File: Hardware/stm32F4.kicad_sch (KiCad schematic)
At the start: 25 parts, among them J1 USB_C_Receptacle_USB2.0_16P, SW1 Push, SW2 Push, U1 STM32F411CCU6, U2 AMS1117-3.3, U3 SRV05-4, Y1 25MHz

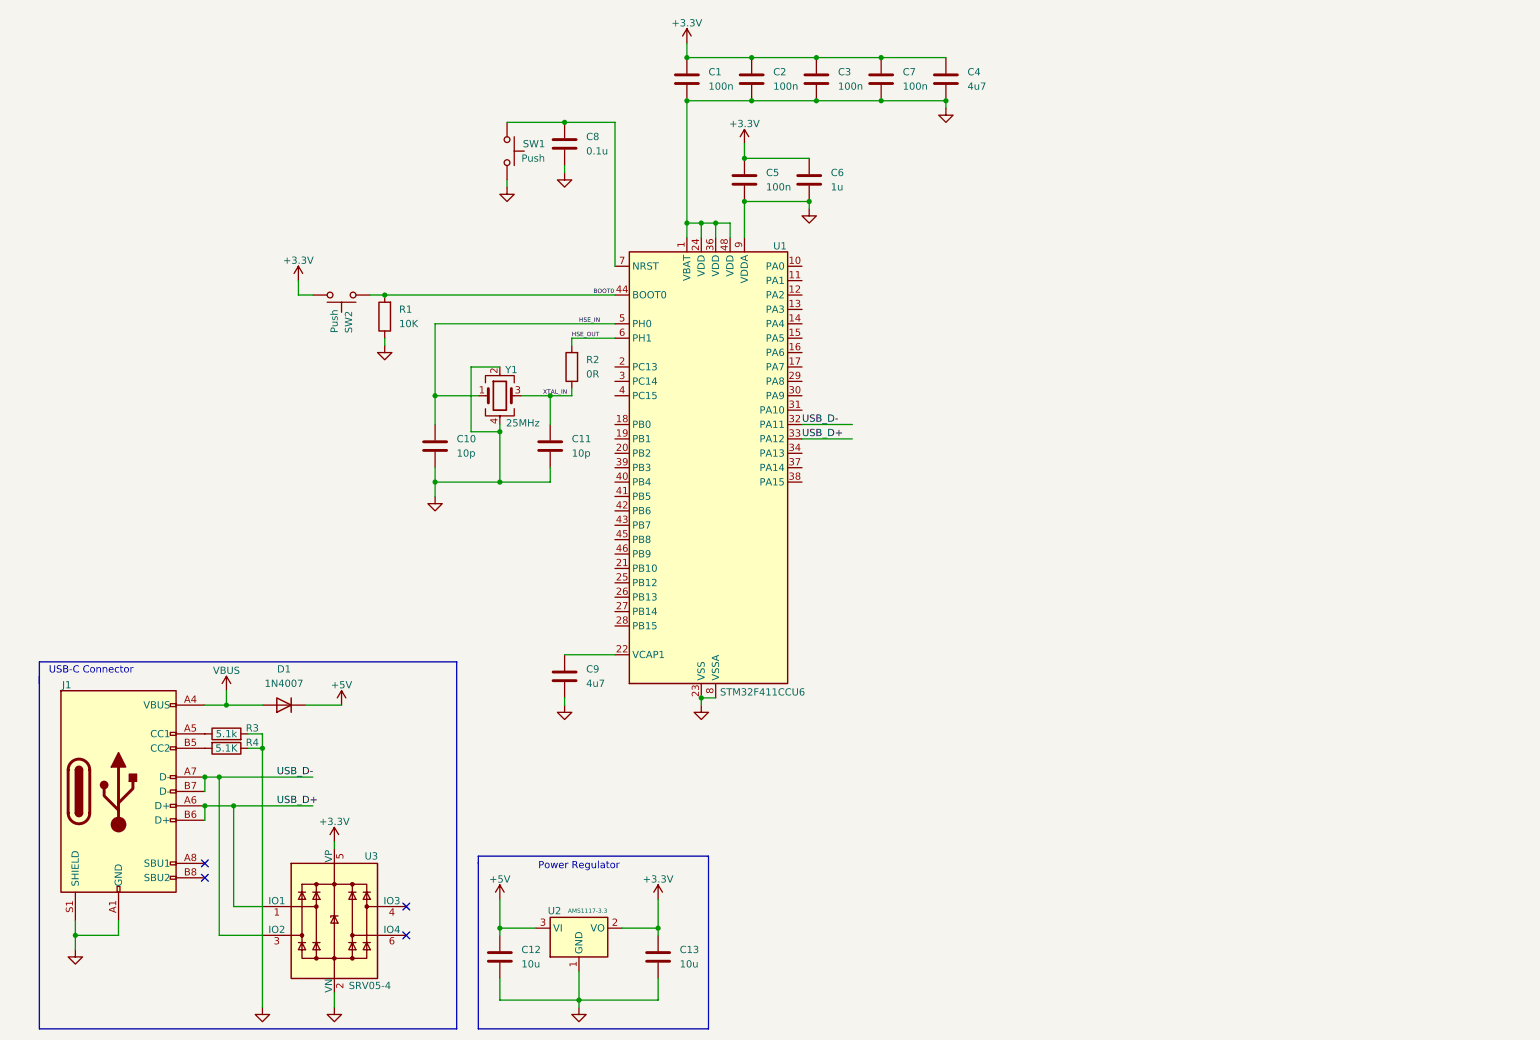
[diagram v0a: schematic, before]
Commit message: Added GPIO Breakout and SWD Conn.
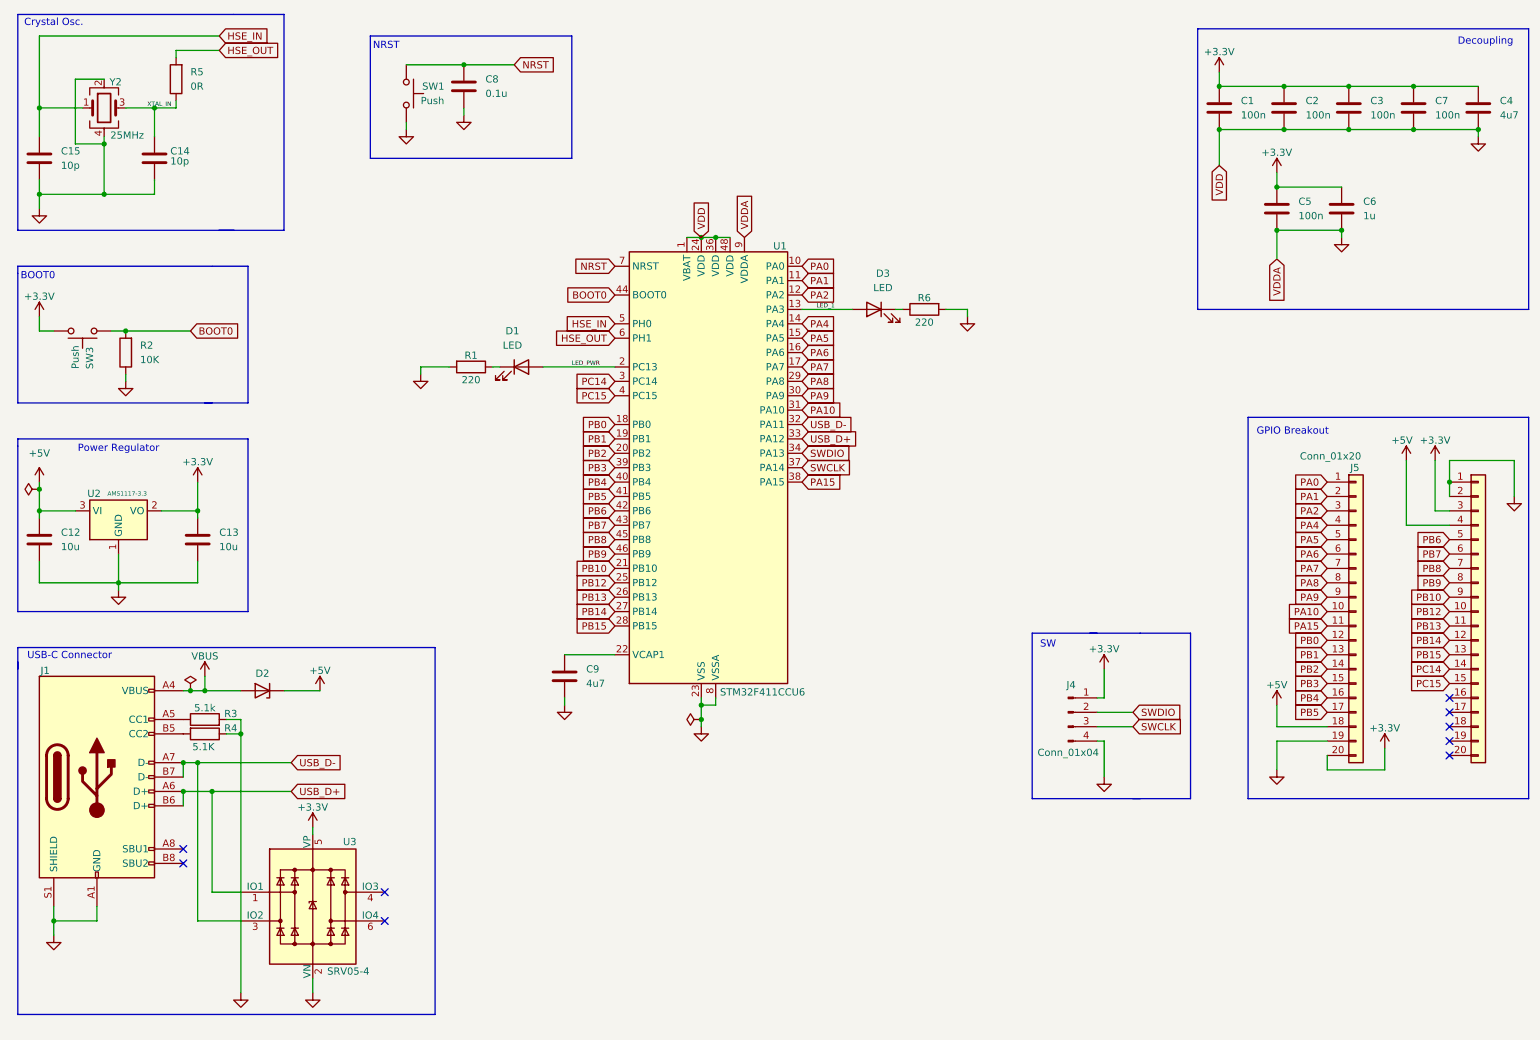
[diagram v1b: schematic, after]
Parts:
- removed C10, C11: 10p, symbol Device:C
- removed D1: 1N4007, Diode_THT:D_DO-41_SOD81_P10.16mm_Horizontal, symbol Diode:1N4007
- removed SW2: Push, symbol Switch:SW_Push
- removed Y1: 25MHz, symbol Device:Crystal_GND24
- added C14, C15: 10p, symbol Device:C
- added D1, D3: LED, symbol Device:LED
- added D2: D_Zener, symbol Device:D_Zener
- added J4: Conn_01x04, Connector_PinHeader_2.54mm:PinHeader_1x04_P2.54mm_Vertical, symbol Connector:Conn_01x04_Pin
- added J5: Conn_01x20, Connector_PinHeader_2.54mm:PinHeader_1x20_P2.54mm_Vertical, symbol Connector_Generic:Conn_01x20
- added J6: Conn_01x20, symbol Connector_Generic:Conn_01x20
- added R5: 0R, symbol Device:R
- added R6: 220, symbol Device:R
- added SW3: Push, symbol Switch:SW_Push
- added Y2: 25MHz, symbol Device:Crystal_GND24
- R1: value 10K -> 220
- R2: value 0R -> 10K
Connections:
- net +3.3V: now also J4.1 (Pin_1), J5.20 (Pin_20), J6.3 (Pin_3), SW3.2
- net +5V: now also D2.1 (K), J5.18 (Pin_18), J6.4 (Pin_4)
- net BOOT0: now also R2.2, SW3.1; no longer R1.2
- net GND: now also R1.2, R2.1, C14.2, C15.2, J4.4 (Pin_4), J5.19 (Pin_19), J6.1 (Pin_1), J6.2 (Pin_2), R6.2, Y2.2, Y2.4; no longer R1.1
- net HSE_IN: now also C15.1, Y2.1
- net HSE_OUT: now also R5.2; no longer R2.2
- net VBUS: now also D2.2 (A)
- net XTAL_IN: now also C14.1, R5.1, Y2.3; no longer R2.1
- net NRST: now reaches C8.2, SW1.1, U1.7 (NRST)
- net PA0: now reaches U1.10 (PA0)
- net PA0: now also J5.1 (Pin_1)
- net PA1: now reaches U1.11 (PA1)
- net PA1: now also J5.2 (Pin_2)
- net PA2: now reaches U1.12 (PA2)
- net PA2: now also J5.3 (Pin_3)
- net LED_1: now reaches U1.13 (PA3)
- net LED_1: now also D3.2 (A)
- net PA4: now reaches U1.14 (PA4)
- net PA4: now also J5.4 (Pin_4)
- net PA5: now reaches U1.15 (PA5)
- net PA5: now also J5.5 (Pin_5)
- net PA6: now reaches U1.16 (PA6)
- net PA6: now also J5.6 (Pin_6)
- net PA7: now reaches U1.17 (PA7)
- net PA7: now also J5.7 (Pin_7)
- net PB0: now reaches U1.18 (PB0)
- net PB0: now also J5.12 (Pin_12)
- net PB1: now reaches U1.19 (PB1)
- net PB1: now also J5.13 (Pin_13)
- net LED_PWR: now reaches U1.2 (PC13)
- net LED_PWR: now also D1.2 (A)
- net PB2: now reaches U1.20 (PB2)
- net PB2: now also J5.14 (Pin_14)
- net PB10: now reaches U1.21 (PB10)
- net PB10: now also J6.9 (Pin_9)
- net PB12: now reaches U1.25 (PB12)
- net PB12: now also J6.10 (Pin_10)
- net PB13: now reaches U1.26 (PB13)
- net PB13: now also J6.11 (Pin_11)
- net PB14: now reaches U1.27 (PB14)
- net PB14: now also J6.12 (Pin_12)
- net PB15: now reaches U1.28 (PB15)
- net PB15: now also J6.13 (Pin_13)
- net PA8: now reaches U1.29 (PA8)
- net PA8: now also J5.8 (Pin_8)
- net PC14: now reaches U1.3 (PC14)
- net PC14: now also J6.14 (Pin_14)
- net PA9: now reaches U1.30 (PA9)
- net PA9: now also J5.9 (Pin_9)
- net PA10: now reaches U1.31 (PA10)
- net PA10: now also J5.10 (Pin_10)
- net SWDIO: now reaches U1.34 (PA13)
- net SWDIO: now also J4.2 (Pin_2)
- net SWCLK: now reaches U1.37 (PA14)
- net SWCLK: now also J4.3 (Pin_3)
- net PA15: now reaches U1.38 (PA15)
- net PA15: now also J5.11 (Pin_11)
- net PB3: now reaches U1.39 (PB3)
- net PB3: now also J5.15 (Pin_15)
- net PC15: now reaches U1.4 (PC15)
- net PC15: now also J6.15 (Pin_15)
- net PB4: now reaches U1.40 (PB4)
- net PB4: now also J5.16 (Pin_16)
- net PB5: now reaches U1.41 (PB5)
- net PB5: now also J5.17 (Pin_17)
- net PB6: now reaches U1.42 (PB6)
- net PB6: now also J6.5 (Pin_5)
- net PB7: now reaches U1.43 (PB7)
- net PB7: now also J6.6 (Pin_6)
- net PB8: now reaches U1.45 (PB8)
- net PB8: now also J6.7 (Pin_7)
- net PB9: now reaches U1.46 (PB9)
- net PB9: now also J6.8 (Pin_8)
- new net: D3.1 (K), R6.1
- new net: D1.1 (K), R1.1
- no-connect marks 4 -> 9
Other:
- note added: "BOOT0"
- note added: "Crystal Osc."
- note added: "Decoupling"
- note added: "GPIO Breakout"
- note added: "NRST"
- note added: "SW"
- title: (none) -> STM32F411 Project
- moved on the sheet: C1, C12, C13, C2, C3, C4, C5, C6, C7, C8, J1, R3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

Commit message: Added Footprints and Parts list
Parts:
- removed D2: D_Zener, symbol Device:D_Zener
- removed J4: Conn_01x04, Connector_PinHeader_2.54mm:PinHeader_1x04_P2.54mm_Vertical, symbol Connector:Conn_01x04_Pin
- removed R5: 0R, symbol Device:R
- removed U3: SRV05-4, Package_TO_SOT_SMD:SOT-23-6, symbol Power_Protection:SRV05-4
- added J2: Conn_01x04, Connector_PinHeader_2.54mm:PinHeader_1x04_P2.54mm_Vertical, symbol Connector_Generic:Conn_01x04
- added U4: 2SC6, Package_TO_SOT_SMD:SOT-23-6, symbol Power_Protection:USBLC6-2SC6
- C1, C2, C3, C5, C7: footprint (none) -> Capacitor_SMD:C_0402_1005Metric; Distributor Link (none) -> https://www.digikey.com/en/products/detail/kyocera-avx/0402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; Manufacturer (none) -> KYOCERA AVX; Manufacturer Part Number (none) -> 04023C104KAT2A-62
- C12, C13: footprint (none) -> Capacitor_SMD:C_0402_1005Metric; Distributor Link (none) -> https://www.digikey.com/en/products/detail/nextgen-componen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; Manufacturer (none) -> Aillen; Manufacturer Part Number (none) -> 0402W106M6R3HI
- C14: value 10p -> 18p; footprint (none) -> Capacitor_SMD:C_0603_1608Metric; Distributor Link (none) -> https://www.digikey.com/en/products/detail/nextgen-componen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; Manufacturer (none) -> NextGen Components; Manufacturer Part Number (none) -> 0603N180J500SD
- C15: value 10p -> 18p; footprint (none) -> Capacitor_SMD:C_0402_1005Metric; Distributor Link (none) -> https://www.digikey.com/en/products/detail/nextgen-componen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; Manufacturer (none) -> NextGen Components; Manufacturer Part Number (none) -> 0603N180J500SD
- C4, C9: footprint (none) -> Capacitor_SMD:C_0603_1608Metric; Distributor Link (none) -> https://www.digikey.com/en/products/detail/tdk-corporation/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; Manufacturer (none) -> TDK Corporation; Manufacturer Part Number (none) -> C1608X5R1C475K080AC
- C6: footprint (none) -> Capacitor_SMD:C_0402_1005Metric; Distributor Link (none) -> https://www.digikey.com/en/products/detail/nextgen-componen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; Manufacturer (none) -> Aillen; Manufacturer Part Number (none) -> 0402W105K100HI
- C8: footprint (none) -> Capacitor_SMD:C_0402_1005Metric; Distributor Link (none) -> https://www.digikey.com/en/products/detail/nextgen-componen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; Manufacturer (none) -> Aillen; Manufacturer Part Number (none) -> 0402B104K160HI
- D1, D3: footprint (none) -> LED_SMD:LED_0402_1005Metric; Distributor Link (none) -> https://www.digikey.com/en/products/detail/yongyu-optoelect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; Manufacturer (none) -> Yongyu Optoelectronics; Manufacturer Part Number (none) -> YY0402RE-NN2S0-T1AR4
- J1: footprint (none) -> Connector_USB:USB_C_Receptacle_GCT_USB4105-xx-A_16P_TopMnt_Horizontal; Distributor Link (none) -> https://www.digikey.com/en/products/detail/gct/USB4105-GF-A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; Manufacturer (none) -> GCT; Manufacturer Part Number (none) -> USB4105-GF-A
- J5: Distributor Link (none) -> https://www.digikey.com/en/products/detail/adam-tech/PH1-20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; Manufacturer (none) -> Adam Tech; Manufacturer Part Number (none) -> PH1-20-UA
- J6: footprint (none) -> Connector_PinHeader_2.54mm:PinHeader_1x20_P2.54mm_Vertical; Distributor Link (none) -> https://www.digikey.com/en/products/detail/adam-tech/PH1-20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; Manufacturer (none) -> Adam Tech; Manufacturer Part Number (none) -> PH1-20-UA
- R1, R6: footprint (none) -> Resistor_SMD:R_0402_1005Metric; Distributor Link (none) -> https://www.digikey.com/en/products/detail/yageo/RC0402FR-0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; Manufacturer (none) -> YAGEO; Manufacturer Part Number (none) -> RC0402FR-07221RL
- R2: footprint (none) -> Resistor_SMD:R_0402_1005Metric; Distributor Link (none) -> https://www.digikey.com/en/products/detail/yageo/RC0402JR-0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; Manufacturer (none) -> YAGEO; Manufacturer Part Number (none) -> RC0402JR-0710KL
- R3, R4: footprint (none) -> Resistor_SMD:R_0402_1005Metric; Distributor Link (none) -> https://www.digikey.com/en/products/detail/yageo/RC0402FR-0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; Manufacturer (none) -> YAGEO; Manufacturer Part Number (none) -> RC0402FR-075K1L
- SW1, SW3: footprint (none) -> Button_Switch_SMD:SW_SPST_CK_RS282G05A3; Distributor Link (none) -> https://www.digikey.com/en/products/detail/c-k/RS-282G05A3-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; Manufacturer (none) -> C&K; Manufacturer Part Number (none) -> RS-282G05A3-SM RT
- U1: Distributor Link (none) -> https://www.digikey.com/en/products/detail/stmicroelectroni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; Manufacturer (none) -> STMicroelectronics; Manufacturer Part Number (none) -> STM32F411CCU6TR
- U2: Distributor Link (none) -> https://www.digikey.com/en/products/detail/umw/AMS1117-3-3/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; Manufacturer (none) -> UMW; Manufacturer Part Number (none) -> AMS1117-3.3
- Y2: value 25MHz -> 8MHz; footprint (none) -> Crystal:Crystal_HC49-4H_Vertical; Distributor Link (none) -> https://www.digikey.com/en/products/detail/ecs-inc/ECS-080-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; Manufacturer (none) -> ECS Inc.; Manufacturer Part Number (none) -> ECS-080-18-5PX-JES-TR
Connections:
- net VBUS is gone; now on net +5V: J1.A4 (VBUS), J1.A9 (VBUS), J1.B4 (VBUS), J1.B9 (VBUS)
- net XTAL_IN is gone; now on net HSE_OUT: C14.1, Y2.3
- net +3.3V: now also J2.1 (Pin_1), U4.5 (VBUS)
- net GND: now also J2.4 (Pin_4), U4.2 (GND)
- net SWCLK: now also J2.3 (Pin_3)
- net SWDIO: now also J2.2 (Pin_2)
- net USB_D+: now also U4.1 (I/O1)
- net USB_D-: now also U4.3 (I/O2)
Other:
- note added: "SWD Header"
- note removed: "SW"

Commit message: Added Net Labels and refined Footprints
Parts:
- J2: footprint Connector_PinHeader_2.54mm:PinHeader_1x04_P2.54mm_Vertical -> Connector_PinHeader_1.27mm:PinHeader_1x04_P1.27mm_Horizontal; Distributor Link https://www.digikey.com/en/products/detail/molex/0530480410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 -> https://www.digikey.com/en/products/detail/sullins-connecto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; Manufacturer Molex -> Sullins Connector Solutions; Manufacturer Part Number 0530480410 -> GRPB041VWCN-RC
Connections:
- net SWCLK renamed SWD_CLK
- net SWDIO renamed SWD_DIO
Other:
- moved on the sheet: C1, C2, C3, C4, C5, C6, C7
